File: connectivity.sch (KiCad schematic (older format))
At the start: 25 parts, among them P1 ADC_CONN, SW1 SW_PUSH, U4 XBee_Header, U5 PCA9685, U6 SN65HVD232D

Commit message: Schematics: Additional I2C connector
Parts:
- added CONN17: I2C, MODULE, symbol I2C
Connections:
- net labels added: I2C1_SCL, I2C1_SDA
- wire segments 105 -> 110
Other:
- moved on the sheet: C6, CONN5, CONN9, U6

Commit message: Schematics: SPI connector
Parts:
- added P?: SPI, symbol CONN_6
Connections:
- net labels added: SPI1_CS1, SPI1_MISO, SPI1_MOSI, SPI1_SCK
- wire segments 110 -> 121
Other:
- note added: "SPI connector"
- moved on the sheet: CONN1, CONN17, CONN5

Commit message: Schematics: Minor cleanups & ADC split between 3.3V & 5V
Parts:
- removed P1: ADC_CONN, symbol CONN_9
- removed P?: SPI, symbol CONN_6
- added CONN18: SPI, _connectors:_Molex-PicoBlade-SMD-6, symbol SPI
- added CONN19: ADC 3.3V, symbol ADC
- added CONN20: ADC 5V, symbol ADC
- added R25, R27, R29: 680, symbol R_Small
- added R26, R28, R30, R32, R34, R36: 820, symbol R_Small
- added R31, R33, R35: 1.47k, symbol R_Small
- C6, R10, R11, R12, R9: footprint (none) -> _std:_0402
- CONN1, CONN17, CONN5, CONN9: footprint MODULE -> _connectors:_Molex-PicoBlade-SMD-4
- CONN10, CONN11, CONN12, CONN13, CONN14, CONN15, CONN2, CONN3, CONN4, CONN6, CONN7, CONN8: footprint (none) -> Pin_Headers:Pin_Header_Straight_1x03
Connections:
- net labels removed: ADC_0, VCC_ADC
- wire segments 121 -> 142
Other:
- note added: "ADC connectors"
- note added: "Use 0.1% resistors for precise readings"
- note removed: "/!\ BEWARE /!\\n\nNo inputs higher \nthan 1.8V or you \nwould blow up the \nBeaglebone's ADC"
- note removed: "ADC connector"
- moved on the sheet: C6, CONN1, CONN10, CONN11, CONN12, CONN13, CONN14, CONN15, CONN17, CONN2, CONN3, CONN4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

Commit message: Netlist
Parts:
- added C23, C24: 100u, Capacitors_SMD:c_elec_6.3x7.7, symbol CP
- C6: footprint _std:_0402 -> Capacitors_SMD:C_0402
- CONN19, CONN20: footprint (none) -> _connectors:_Molex-PicoBlade-SMD-4
- R10, R11, R12, R9: footprint _std:_0402 -> Resistors_SMD:R_0402
- R25, R26, R27, R28, R29, R30, R31, R32, R33, R34, R35, R36: footprint (none) -> Resistors_SMD:R_0402
- SW1: footprint (none) -> _div:_PTS525SK15-SMT-Pushbutton
- U4: footprint (none) -> _connectors:XBEE-HEADER
- U5: footprint (none) -> Housings_DFN_QFN:QFN-28-1EP_6x6mm_Pitch0.65mm
- U6: footprint (none) -> SMD_Packages:SOIC-8-N
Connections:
- net GND: now also C23.2, C24.2
- net POWER: now also C23.1, C24.1

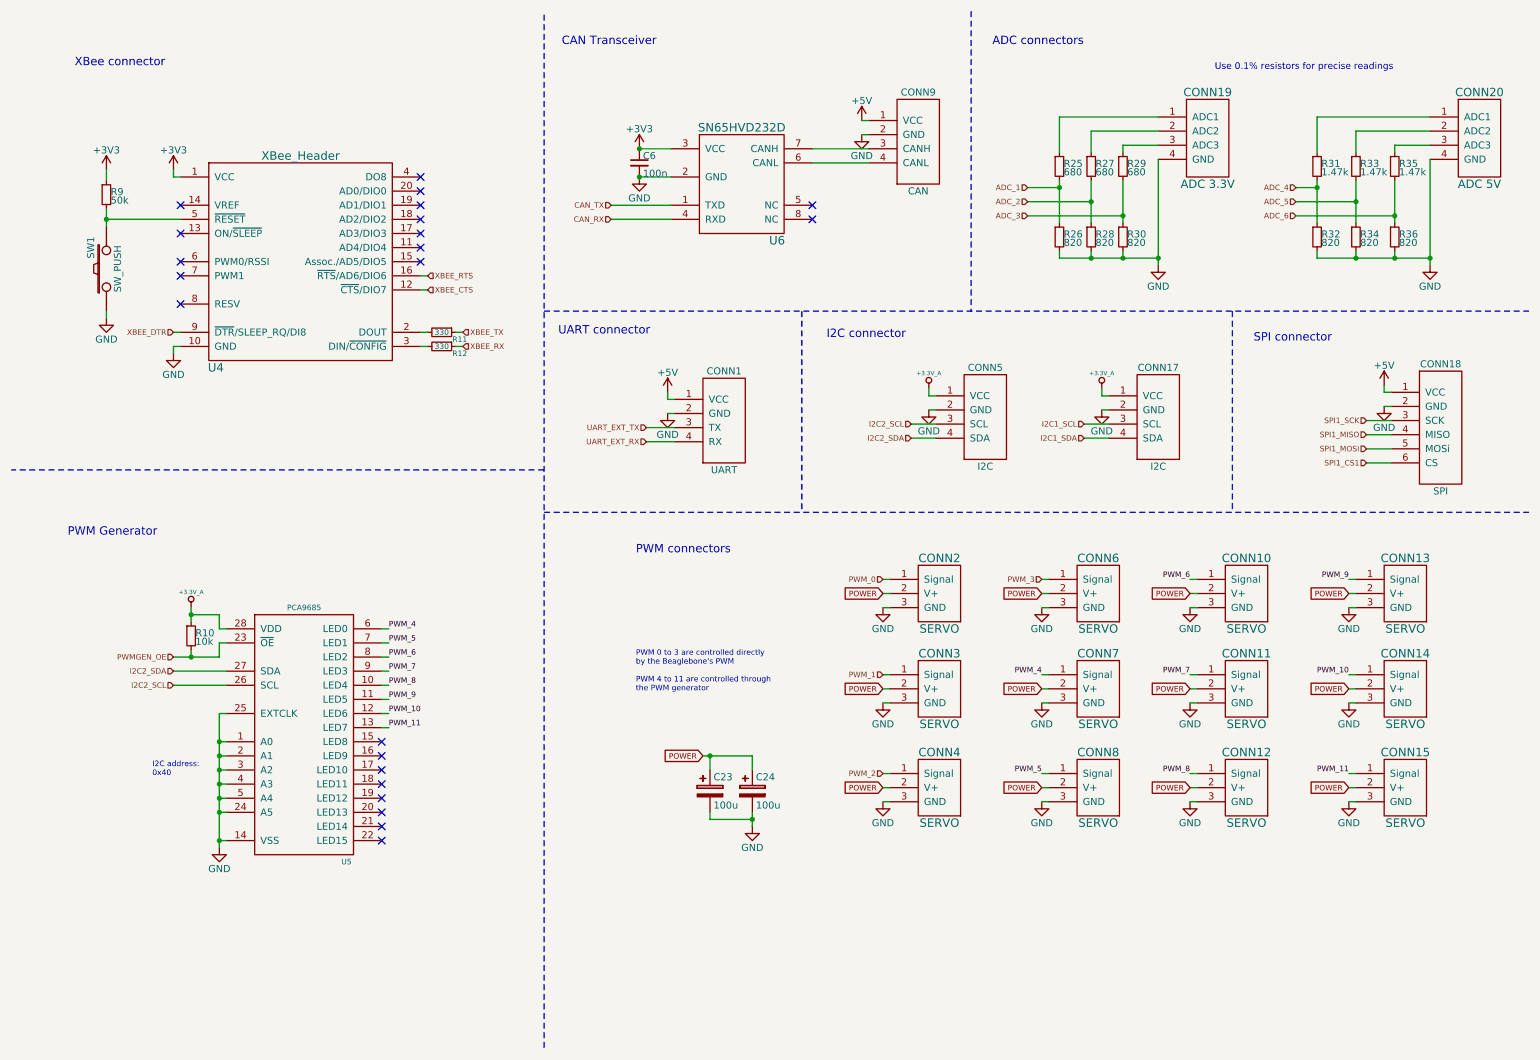
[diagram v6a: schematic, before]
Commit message: Schematics: CAN termination resistor + PWM gen decoupling cap
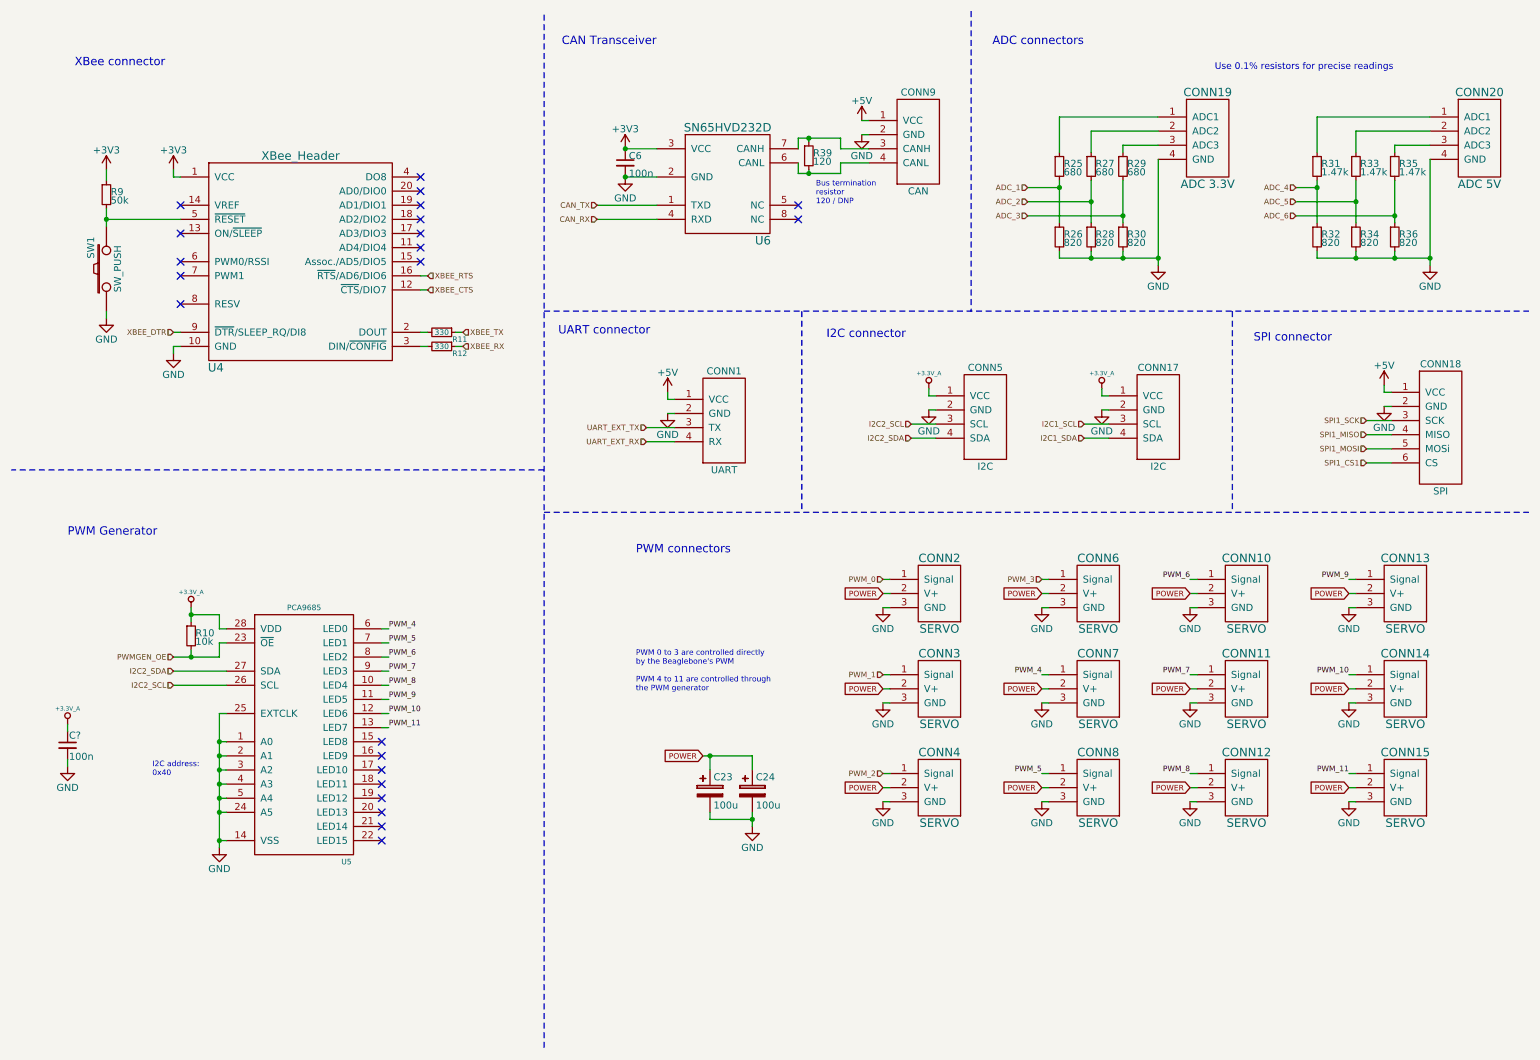
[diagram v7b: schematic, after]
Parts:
- added C?: 100n, symbol C_Small
- added R39: 120, Resistors_SMD:R_0402, symbol R_Small
- U4: footprint _connectors:XBEE-HEADER -> _connectors:Xbee_Header_SMD
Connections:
- net +3.3V_A: now also C?.1
- net GND: now also C?.2
- net at CONN9.4 (CANL), U6.6 (CANL): now also R39.2
- net at CONN9.3 (CANH), U6.7 (CANH): now also R39.1
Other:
- note added: "Bus termination \nresistor\n120 / DNP"
- moved on the sheet: C6, U6
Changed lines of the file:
@@
 F 0 "U4" H 1925 1475 60  0000 C CNN
 F 1 "XBee_Header" H 2525 2975 60  0000 C CNN
-F 2 "_connectors:XBEE-HEADER" H 2275 2225 60  0001 C CNN
+F 2 "_connectors:Xbee_Header_SMD" H 2275 2225 60  0001 C CNN
 F 3 "" H 2275 2225 60  0000 C CNN
 	1    2525 2225
@@
 L SN65HVD232D U6
 U 1 1 55AABB00
-P 5650 1625
-F 0 "U6" H 5900 1175 60  0000 C CNN
-F 1 "SN65HVD232D" H 5650 1975 60  0000 C CNN
-F 2 "SMD_Packages:SOIC-8-N" H 5650 1625 60  0001 C CNN
-F 3 "" H 5650 1625 60  0000 C CNN
-	1    5650 1625
+P 5550 1625
+F 0 "U6" H 5800 1175 60  0000 C CNN
+F 1 "SN65HVD232D" H 5550 1975 60  0000 C CNN
+F 2 "SMD_Packages:SOIC-8-N" H 5550 1625 60  0001 C CNN
+F 3 "" H 5550 1625 60  0000 C CNN
+	1    5550 1625
 	1    0    0    -1
 $EndComp
@@
 L C_Small C6
 U 1 1 55AABD28
-P 4925 1525
-F 0 "C6" H 4950 1575 50  0000 L CNN
-F 1 "100n" H 4950 1450 50  0000 L CNN
-F 2 "Capacitors_SMD:C_0402" H 4925 1525 60  0001 C CNN
-F 3 "" H 4925 1525 60  0000 C CNN
-	1    4925 1525
+P 4825 1525
+F 0 "C6" H 4850 1575 50  0000 L CNN
+F 1 "100n" H 4850 1450 50  0000 L CNN
+F 2 "Capacitors_SMD:C_0402" H 4825 1525 60  0001 C CNN
+F 3 "" H 4825 1525 60  0000 C CNN
+	1    4825 1525
 	1    0    0    -1
 $EndComp
@@
 L GND #PWR047
 U 1 1 55AABF17
-P 4925 1625
-F 0 "#PWR047" H 4925 1375 50  0001 C CNN
-F 1 "GND" H 4925 1475 50  0000 C CNN
-F 2 "" H 4925 1625 60  0000 C CNN
-F 3 "" H 4925 1625 60  0000 C CNN
-	1    4925 1625
+P 4825 1625
+F 0 "#PWR047" H 4825 1375 50  0001 C CNN
+F 1 "GND" H 4825 1475 50  0000 C CNN
+F 2 "" H 4825 1625 60  0000 C CNN
+F 3 "" H 4825 1625 60  0000 C CNN
+	1    4825 1625
 	1    0    0    -1
 $EndComp
@@
 L +3V3 #PWR048
 U 1 1 55AABF5B
-P 4925 1425
-F 0 "#PWR048" H 4925 1275 50  0001 C CNN
-F 1 "+3V3" H 4925 1565 50  0000 C CNN
-F 2 "" H 4925 1425 60  0000 C CNN
-F 3 "" H 4925 1425 60  0000 C CNN
-	1    4925 1425
-	1    0    0    -1
-$EndComp
-NoConn ~ 6150 1825
-NoConn ~ 6150 1925
+P 4825 1425
+F 0 "#PWR048" H 4825 1275 50  0001 C CNN
+F 1 "+3V3" H 4825 1565 50  0000 C CNN
+F 2 "" H 4825 1425 60  0000 C CNN
+F 3 "" H 4825 1425 60  0000 C CNN
+	1    4825 1425
+	1    0    0    -1
+$EndComp
+NoConn ~ 6050 1825
+NoConn ~ 6050 1925
 $Comp
 L +5V #PWR049
@@
 	1    0    0    -1
 $EndComp
-Text HLabel 4725 1825 0    39   Input ~ 0
+Text HLabel 4625 1825 0    39   Input ~ 0
 CAN_TX
-Text HLabel 4725 1925 0    39   Input ~ 0
+Text HLabel 4625 1925 0    39   Input ~ 0
 CAN_RX
 Text Label 7775 5150 2    39   ~ 0
@@
 Text Notes 9000 875  0    47   ~ 0
 Use 0.1% resistors for precise readings
+$Comp
+L CP C23
+U 1 1 55B4EF1A
+P 5425 5975
+F 0 "C23" H 5450 6075 50  0000 L CNN
+F 1 "100u" H 5450 5875 50  0000 L CNN
+F 2 "Capacitors_SMD:c_elec_6.3x7.7" H 5463 5825 30  0001 C CNN
+F 3 "" H 5425 5975 60  0000 C CNN
+	1    5425 5975
+	1    0    0    -1
+$EndComp
+Text GLabel 5375 5725 0    39   Input ~ 0
+POWER
+$Comp
+L GND #PWR061
+U 1 1 55B4F1B2
+P 5725 6225
+F 0 "#PWR061" H 5725 5975 50  0001 C CNN
+F 1 "GND" H 5725 6075 50  0000 C CNN
+F 2 "" H 5725 6225 60  0000 C CNN
+F 3 "" H 5725 6225 60  0000 C CNN
+	1    5725 6225
+	1    0    0    -1
+$EndComp
+$Comp
+L CP C24
+U 1 1 55B4F885
+P 5725 5975
+F 0 "C24" H 5750 6075 50  0000 L CNN
+F 1 "100u" H 5750 5875 50  0000 L CNN
+F 2 "Capacitors_SMD:c_elec_6.3x7.7" H 5763 5825 30  0001 C CNN
+F 3 "" H 5725 5975 60  0000 C CNN
+	1    5725 5975
+	1    0    0    -1
+$EndComp
+$Comp
+L R_Small R39
+U 1 1 55AE6735
+P 6125 1475
+F 0 "R39" H 6155 1495 50  0000 L CNN
+F 1 "120" H 6155 1435 50  0000 L CNN
+F 2 "Resistors_SMD:R_0402" H 6125 1475 60  0001 C CNN
+F 3 "" H 6125 1475 60  0000 C CNN
+	1    6125 1475
+	1    0    0    -1
+$EndComp
+Text Notes 6175 1825 0    39   ~ 0
+Bus termination \nresistor\n120 / DNP
+$Comp
+L C_Small C?
+U 1 1 55AE8752
+P 875 5650
+F 0 "C?" H 885 5720 50  0000 L CNN
+F 1 "100n" H 885 5570 50  0000 L CNN
+F 2 "" H 875 5650 60  0000 C CNN
+F 3 "" H 875 5650 60  0000 C CNN
+	1    875  5650
+	1    0    0    -1
+$EndComp
 Wire Wire Line
 	3425 2725 3375 2725
@@
 	3100 5125 3150 5125
 Wire Wire Line
-	5150 1425 4925 1425
-Wire Wire Line
-	4925 1625 5150 1625
-Connection ~ 4925 1625
-Connection ~ 4925 1425
-Wire Wire Line
-	6150 1425 6550 1425
-Wire Wire Line
-	6550 1525 6150 1525
+	5050 1425 4825 1425
+Wire Wire Line
+	4825 1625 5050 1625
+Connection ~ 4825 1625
+Connection ~ 4825 1425
 Wire Wire Line
 	6500 1225 6550 1225
@@
 	6500 1325 6550 1325
 Wire Wire Line
-	4725 1825 5150 1825
-Wire Wire Line
-	4725 1925 5150 1925
+	4625 1825 5050 1825
+Wire Wire Line
+	4625 1925 5050 1925
 Wire Wire Line
 	3150 4825 3100 4825
@@
 Wire Notes Line
 	4250 4000 11225 4000
-$Comp
-L CP C23
-U 1 1 55B4EF1A
-P 5425 5975
-F 0 "C23" H 5450 6075 50  0000 L CNN
-F 1 "100u" H 5450 5875 50  0000 L CNN
-F 2 "Capacitors_SMD:c_elec_6.3x7.7" H 5463 5825 30  0001 C CNN
-F 3 "" H 5425 5975 60  0000 C CNN
-	1    5425 5975
-	1    0    0    -1
-$EndComp
-Text GLabel 5375 5725 0    39   Input ~ 0
-POWER
 Wire Wire Line
 	5375 5725 5725 5725
 Wire Wire Line
 	5425 5725 5425 5825
-$Comp
-L GND #PWR061
-U 1 1 55B4F1B2
-P 5725 6225
-F 0 "#PWR061" H 5725 5975 50  0001 C CNN
-F 1 "GND" H 5725 6075 50  0000 C CNN
-F 2 "" H 5725 6225 60  0000 C CNN
-F 3 "" H 5725 6225 60  0000 C CNN
-	1    5725 6225
-	1    0    0    -1
-$EndComp
 Wire Wire Line
 	5425 6175 5425 6125
-$Comp
-L CP C24
-U 1 1 55B4F885
-P 5725 5975
-F 0 "C24" H 5750 6075 50  0000 L CNN
-F 1 "100u" H 5750 5875 50  0000 L CNN
-F 2 "Capacitors_SMD:c_elec_6.3x7.7" H 5763 5825 30  0001 C CNN
-F 3 "" H 5725 5975 60  0000 C CNN
-	1    5725 5975
-	1    0    0    -1
-$EndComp
 Wire Wire Line
 	5725 5725 5725 5825
@@
 	5425 6175 5725 6175
 Connection ~ 5725 6175
+Wire Wire Line
+	6050 1425 6050 1350
+Wire Wire Line
+	6050 1350 6350 1350
+Wire Wire Line
+	6125 1350 6125 1375
+Wire Wire Line
+	6050 1525 6050 1600
+Wire Wire Line
+	6050 1600 6350 1600
+Wire Wire Line
+	6125 1600 6125 1575
+Wire Wire Line
+	6350 1600 6350 1525
+Wire Wire Line
+	6350 1525 6550 1525
+Connection ~ 6125 1600
+Wire Wire Line
+	6550 1425 6350 1425
+Wire Wire Line
+	6350 1425 6350 1350
+Connection ~ 6125 1350
+$Comp
+L +3.3V_A #PWR?
+U 1 1 55AE8E8A
+P 875 5500
+F 0 "#PWR?" H 875 5460 30  0001 C CNN
+F 1 "+3.3V_A" H 875 5610 30  0000 C CNN
+F 2 "" H 875 5500 60  0000 C CNN
+F 3 "" H 875 5500 60  0000 C CNN
+	1    875  5500
+	1    0    0    -1
+$EndComp
+$Comp
+L GND #PWR?
+U 1 1 55AE8F19
+P 875 5800
+F 0 "#PWR?" H 875 5550 50  0001 C CNN
+F 1 "GND" H 875 5650 50  0000 C CNN
+F 2 "" H 875 5800 60  0000 C CNN
+F 3 "" H 875 5800 60  0000 C CNN
+	1    875  5800
+	1    0    0    -1
+$EndComp
+Wire Wire Line
+	875  5800 875  5750
+Wire Wire Line
+	875  5500 875  5550
 $EndSCHEMATC

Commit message: PCB: Layout of close tracks
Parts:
- C25: renamed from C?; footprint (none) -> Capacitors_SMD:C_0402
- CONN18: footprint _connectors:_Molex-PicoBlade-SMD-6 -> (none)
- CONN19, CONN20: footprint _connectors:_Molex-PicoBlade-SMD-4 -> (none)
